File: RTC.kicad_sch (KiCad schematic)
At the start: 11 parts, among them J12 RTC Battery Port, J13 RTC Battery Conn, J7 Molex 470531000, U1 RTC PCF8563T, U10 Fan PWM Controller, Y6 ECS-.327-6

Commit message: moved some stuff around
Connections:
- net +12V_PWR renamed +24V_PWR
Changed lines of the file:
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@@
 		)
 	)
-	(hierarchical_label "+12V_PWR"
+	(hierarchical_label "+24V_PWR"
 		(shape input)
 		(at 233.68 118.11 180)

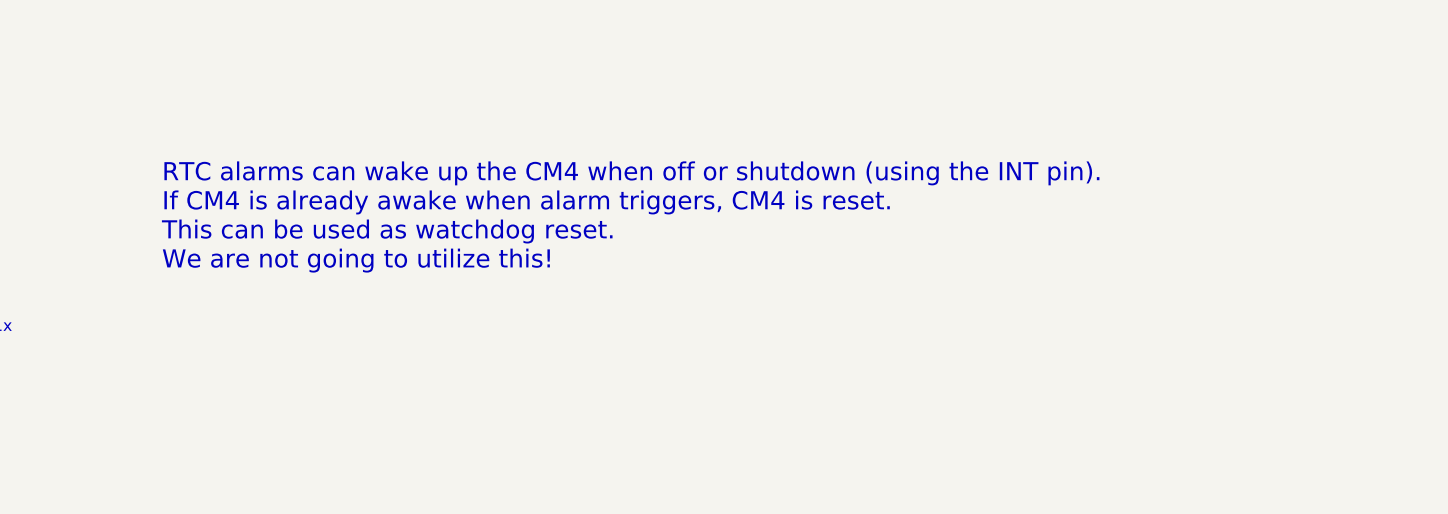
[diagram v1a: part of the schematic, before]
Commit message: Migrate to USB C and added some ESD protections on Vbus; might still have some issues
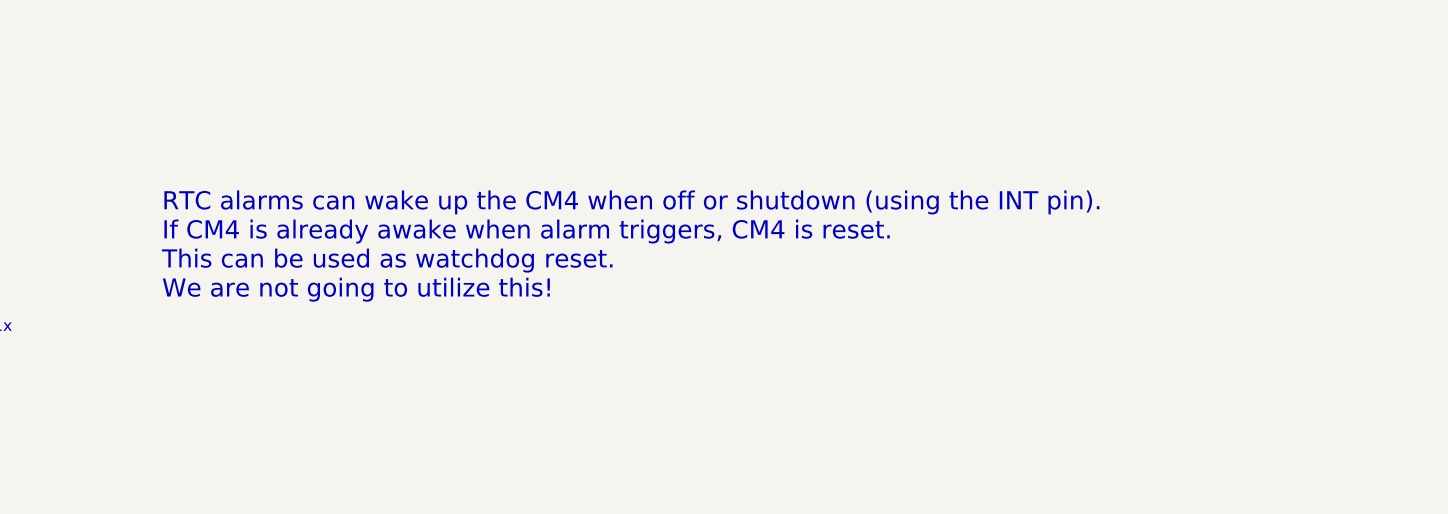
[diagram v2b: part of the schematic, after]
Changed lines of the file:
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@@
 (kicad_sch
-	(version 20231120)
+	(version 20250114)
 	(generator "eeschema")
-	(generator_version "8.0")
+	(generator_version "9.0")
 	(paper "A4")
+	(text "FAN connector\n"
+		(exclude_from_sim no)
+		(at 240.03 113.03 0)
+		(effects
+			(font
+				(size 1.27 1.27)
+			)
+			(justify left bottom)
+		)
+	)
+	(text "Also SMBUS alert IIC address : 0001_100x"
+		(exclude_from_sim no)
+		(at 184.1754 134.8994 0)
+		(effects
+			(font
+				(size 1.27 1.27)
+			)
+			(justify left bottom)
+		)
+	)
+	(text "IIC address : 1010_001x"
+		(exclude_from_sim no)
+		(at 91.3638 65.9638 0)
+		(effects
+			(font
+				(size 1.27 1.27)
+			)
+			(justify left bottom)
+		)
+	)
+	(text "Battery is enclosed in a non-SMD holder to mitigate vibration concerns. This is \ntechnically an off-board section that has the 2032 coin cell, the battery holder, \nand the molex connector (male)."
+		(exclude_from_sim no)
+		(at 39.37 120.65 0)
+		(effects
+			(font
+				(size 1.27 1.27)
+			)
+			(justify left)
+		)
+	)
+	(text "FAN controller"
+		(exclude_from_sim no)
+		(at 165.1 93.98 0)
+		(effects
+			(font
+				(size 2.0066 2.0066)
+			)
+			(justify left bottom)
+		)
+	)
+	(text "RTC alarms can wake up the CM4 when off or shutdown (using the INT pin).\nIf CM4 is already awake when alarm triggers, CM4 is reset.\nThis can be used as watchdog reset.\nWe are not going to utilize this!"
+		(exclude_from_sim no)
+		(at 129.032 62.23 0)
+		(effects
+			(font
+				(size 2.0066 2.0066)
+			)
+			(justify left bottom)
+		)
+	)
+	(text "RTC and RTC wakeup"
+		(exclude_from_sim no)
+		(at 58.928 34.29 0)
+		(effects
+			(font
+				(size 2.0066 2.0066)
+			)
+			(justify left bottom)
+		)
+	)
+	(text "IIC address : 0101_111x"
+		(exclude_from_sim no)
+		(at 184.15 130.81 0)
+		(effects
+			(font
+				(size 1.27 1.27)
+			)
+			(justify left bottom)
+		)
+	)
 	(junction
 		(at 207.01 120.65)
@@
 		)
 	)
-	(text "FAN connector\n"
-		(exclude_from_sim no)
-		(at 240.03 113.03 0)
-		(effects
-			(font
-				(size 1.27 1.27)
-			)
-			(justify left bottom)
-		)
-	)
-	(text "Also SMBUS alert IIC address : 0001_100x"
-		(exclude_from_sim no)
-		(at 184.1754 134.8994 0)
-		(effects
-			(font
-				(size 1.27 1.27)
-			)
-			(justify left bottom)
-		)
-	)
-	(text "IIC address : 1010_001x"
-		(exclude_from_sim no)
-		(at 91.3638 65.9638 0)
-		(effects
-			(font
-				(size 1.27 1.27)
-			)
-			(justify left bottom)
-		)
-	)
-	(text "Battery is enclosed in a non-SMD holder to mitigate vibration concerns. This is \ntechnically an off-board section that has the 2032 coin cell, the battery holder, \nand the molex connector (male)."
-		(exclude_from_sim no)
-		(at 39.37 120.65 0)
-		(effects
-			(font
-				(size 1.27 1.27)
-			)
-			(justify left)
-		)
-	)
-	(text "FAN controller"
-		(exclude_from_sim no)
-		(at 165.1 93.98 0)
-		(effects
-			(font
-				(size 2.0066 2.0066)
-			)
-			(justify left bottom)
-		)
-	)
-	(text "RTC alarms can wake up the CM4 when off or shutdown (using the INT pin).\nIf CM4 is already awake when alarm triggers, CM4 is reset.\nThis can be used as watchdog reset.\nWe are not going to utilize this!\n\n"
-		(exclude_from_sim no)
-		(at 129.032 62.23 0)
-		(effects
-			(font
-				(size 2.0066 2.0066)
-			)
-			(justify left bottom)
-		)
-	)
-	(text "RTC and RTC wakeup"
-		(exclude_from_sim no)
-		(at 58.928 34.29 0)
-		(effects
-			(font
-				(size 2.0066 2.0066)
-			)
-			(justify left bottom)
-		)
-	)
-	(text "IIC address : 0101_111x"
-		(exclude_from_sim no)
-		(at 184.15 130.81 0)
-		(effects
-			(font
-				(size 1.27 1.27)
-			)
-			(justify left bottom)
-		)
-	)
 	(label "RED"
 		(at 39.37 66.04 0)
-		(fields_autoplaced yes)
 		(effects
 			(font
@@
 	(label "BLK"
 		(at 72.39 114.3 90)
-		(fields_autoplaced yes)
 		(effects
 			(font
@@
 	(label "BLK"
 		(at 39.37 68.58 0)
-		(fields_autoplaced yes)
 		(effects
 			(font
@@
 	(label "RED"
 		(at 72.39 96.52 270)
-		(fields_autoplaced yes)
 		(effects
 			(font
@@
 		(shape input)
 		(at 173.99 115.57 180)
-		(fields_autoplaced yes)
 		(effects
 			(font
@@
 		(shape input)
 		(at 173.99 118.11 180)
-		(fields_autoplaced yes)
 		(effects
 			(font
@@
 		(shape input)
 		(at 233.68 118.11 180)
-		(fields_autoplaced yes)
 		(effects
 			(font
@@
 		(shape input)
 		(at 163.83 100.33 0)
-		(fields_autoplaced yes)
 		(effects
 			(font
@@
 		(shape input)
 		(at 101.6 50.8 0)
-		(fields_autoplaced yes)
 		(effects
 			(font
@@
 		(shape input)
 		(at 36.83 40.64 180)
-		(fields_autoplaced yes)
 		(effects
 			(font
@@
 		(shape input)
 		(at 101.6 48.26 0)
-		(fields_autoplaced yes)
-		(effects
-			(font
+		(effects
+			(font

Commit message: fixed erc and removed old schematics
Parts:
- J13: footprint (none) -> CONN02_530470210_MOL
- Y6: Arrow Part Number (none) -> ECS-.327-6-16R-TR; Arrow Price/Stock (none) -> https://www.arrow.com/en/products/ecs-.327-6-16r-tr/ecs-int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; Height (none) -> 0.5; Manufacturer_Name (none) -> ECS; Manufacturer_Part_Number (none) -> ECS-.327-6-16R-TR; Mouser Part Number (none) -> 520-ECS-.327-6-16RTR; Mouser Price/Stock (none) -> https://www.mouser.co.uk/ProductDetail/ECS/ECS-.327-6-16R-T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
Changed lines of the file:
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@@
 	)
 	(symbol
-		(lib_name "GND_1")
 		(lib_id "power:GND")
 		(at 39.37 72.39 0)
@@
 			)
 		)
-		(property "Footprint" ""
+		(property "Footprint" "CONN02_530470210_MOL"
 			(at 77.47 104.14 0)
 			(effects
@@
 			)
 		)
-		(property "Datasheet" "https://www.molex.com/en-us/products/part-detail-pdf/510210200?display=pdf"
+		(property "Datasheet" "https://tools.molex.com/pdm_docs/ps/PS-51021-009.pdf"
 			(at 77.47 104.14 0)
 			(effects
@@
 			)
 		)
+		(property "Height" "0.5"
+			(at -332.69 57.15 0)
+			(effects
+				(font
+					(size 1.27 1.27)
+				)
+				(justify left top)
+				(hide yes)
+			)
+		)
+		(property "Manufacturer_Name" "ECS"
+			(at -432.69 57.15 0)
+			(effects
+				(font
+					(size 1.27 1.27)
+				)
+				(justify left top)
+				(hide yes)
+			)
+		)
+		(property "Manufacturer_Part_Number" "ECS-.327-6-16R-TR"
+			(at -532.69 57.15 0)
+			(effects
+				(font
+					(size 1.27 1.27)
+				)
+				(justify left top)
+				(hide yes)
+			)
+		)
+		(property "Mouser Part Number" "520-ECS-.327-6-16RTR"
+			(at -632.69 57.15 0)
+			(effects
+				(font
+					(size 1.27 1.27)
+				)
+				(justify left top)
+				(hide yes)
+			)
+		)
+		(property "Mouser Price/Stock" "https://www.mouser.co.uk/ProductDetail/ECS/ECS-.327-6-16R-TR?qs=hWgE7mdIu5R4lQOKQkWLTw%3D%3D"
+			(at -732.69 57.15 0)
+			(effects
+				(font
+					(size 1.27 1.27)
+				)
+				(justify left top)
+				(hide yes)
+			)
+		)
+		(property "Arrow Part Number" "ECS-.327-6-16R-TR"
+			(at -832.69 57.15 0)
+			(effects
+				(font
+					(size 1.27 1.27)
+				)
+				(justify left top)
+				(hide yes)
+			)
+		)
+		(property "Arrow Price/Stock" "https://www.arrow.com/en/products/ecs-.327-6-16r-tr/ecs-international?region=nac"
+			(at -932.69 57.15 0)
+			(effects
+				(font
+					(size 1.27 1.27)
+				)
+				(justify left top)
+				(hide yes)
+			)
+		)
 		(pin "2"
 		)
@@
 	)
 	(symbol
-		(lib_name "GND_4")
 		(lib_id "power:GND")
 		(at 82.55 66.04 0)
@@
 	)
 	(symbol
-		(lib_name "GND_1")
 		(lib_id "power:GND")
 		(at 54.61 54.61 0)
@@
 	)
 	(symbol
-		(lib_name "GND_4")
 		(lib_id "power:GND")
 		(at 240.03 132.08 0)
@@
 			)
 		)
-		(property "Datasheet" "https://www.mouser.com/datasheet/2/215/1086-1901326.pdf"
+		(property "Datasheet" "https://www.keyelco.com/product-pdf.cfm?p=14638"
 			(at 72.39 105.156 90)
 			(effects
@@
 			)
 		)
-		(property "Description" "Single-cell battery holder"
+		(property "Description" "Single-cell battery Holder 20mm 6\" leads"
 			(at 72.39 106.68 0)
 			(effects
@@
 	)
 	(symbol
-		(lib_name "PCF8563T_1")
 		(lib_id "Timer_RTC:PCF8563T")
 		(at 82.55 53.34 0)
@@
 	)
 	(symbol
-		(lib_name "GND_3")
 		(lib_id "power:GND")
 		(at 168.91 132.08 0)
@@
 			)
 		)
-		(property "Datasheet" "https://www.mouser.com/datasheet/2/447/KEM_C1002_X7R_SMD-3316098.pdf"
+		(property "Datasheet" "~"
 			(at 54.61 48.26 0)
 			(effects
@@
 			)
 		)
-		(property "Description" "Capacitor 0.1u 20%"
+		(property "Description" "Unpolarized capacitor"
 			(at 54.61 48.26 0)
 			(effects
@@
 	)
 	(symbol
-		(lib_name "530470210_1")
 		(lib_id "530470210:530470210")
 		(at 46.99 66.04 0)
@@
 			)
 		)
-		(property "Datasheet" "530470210"
+		(property "Datasheet" "https://www.molex.com/content/dam/molex/molex-dot-com/products/automated/en-us/salesdrawingpdf/530/53047/530470210_sd.pdf?inline"
 			(at 46.99 66.04 0)
 			(effects
@@
 	)
 	(symbol
-		(lib_name "GND_4")
 		(lib_id "power:GND")
 		(at 179.07 132.08 0)
@@
 			)
 		)
-		(property "Datasheet" "https://www.mouser.com/datasheet/2/447/PYu_AC_51_RoHS_L_11-3418659.pdf"
+		(property "Datasheet" "~"
 			(at 207.01 115.57 0)
 			(effects
@@
 			)
 		)
-		(property "Description" "Resistor 36K M1005 1% 125mW"
+		(property "Description" "Resistor"
 			(at 207.01 115.57 0)
 			(effects
@@
 			)
 		)
-		(property "Datasheet" "https://www.mouser.com/datasheet/2/447/KEM_C1002_X7R_SMD-3316098.pdf"
+		(property "Datasheet" "~"
 			(at 168.91 127 0)
 			(effects
@@
 			)
 		)
-		(property "Description" "Capacitor 0.1u 20%"
+		(property "Description" "Unpolarized capacitor"
 			(at 168.91 127 0)
 			(effects
@@
 			)
 		)
-		(property "Datasheet" "https://www.molex.com/en-us/products/part-detail/470531000?display=pdf"
+		(property "Datasheet" "~"
 			(at 246.38 118.11 0)
 			(effects
@@
 			)
 		)
-		(property "Description" "Connector Header Through Hole 4 position 0.100\" (2.54mm)"
+		(property "Description" "Generic connector, single row, 01x04, script generated (kicad-library-utils/schlib/autogen/connector/)"
 			(at 246.38 118.11 0)
 			(effects

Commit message: changed usb to be simpler (no inbuilt hub)
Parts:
- J12, J13: footprint CONN02_530470210_MOL -> Controls_Pi:CONN02_530470210_MOL
- Y6: Arrow Part Number ECS-.327-6-16R-TR -> (none); Arrow Price/Stock https://www.arrow.com/en/products/ecs-.327-6-16r-tr/ecs-int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 -> (none); Height 0.5 -> (none); Manufacturer_Name ECS -> (none); Manufacturer_Part_Number ECS-.327-6-16R-TR -> (none); Mouser Part Number 520-ECS-.327-6-16RTR -> (none); Mouser Price/Stock https://www.mouser.co.uk/ProductDetail/ECS/ECS-.327-6-16R-T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 -> (none)
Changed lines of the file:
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@@
 			)
 		)
-		(property "Footprint" "CONN02_530470210_MOL"
+		(property "Footprint" "Controls_Pi:CONN02_530470210_MOL"
 			(at 77.47 104.14 0)
 			(effects
@@
 		(property "P/N" "ECS-.327-6-16R-TR"
 			(at -532.69 57.15 0)
-			(effects
-				(font
-					(size 1.27 1.27)
-				)
-				(justify left top)
-				(hide yes)
-			)
-		)
-		(property "Height" "0.5"
-			(at -332.69 57.15 0)
-			(effects
-				(font
-					(size 1.27 1.27)
-				)
-				(justify left top)
-				(hide yes)
-			)
-		)
-		(property "Manufacturer_Name" "ECS"
-			(at -432.69 57.15 0)
-			(effects
-				(font
-					(size 1.27 1.27)
-				)
-				(justify left top)
-				(hide yes)
-			)
-		)
-		(property "Manufacturer_Part_Number" "ECS-.327-6-16R-TR"
-			(at -532.69 57.15 0)
-			(effects
-				(font
-					(size 1.27 1.27)
-				)
-				(justify left top)
-				(hide yes)
-			)
-		)
-		(property "Mouser Part Number" "520-ECS-.327-6-16RTR"
-			(at -632.69 57.15 0)
-			(effects
-				(font
-					(size 1.27 1.27)
-				)
-				(justify left top)
-				(hide yes)
-			)
-		)
-		(property "Mouser Price/Stock" "https://www.mouser.co.uk/ProductDetail/ECS/ECS-.327-6-16R-TR?qs=hWgE7mdIu5R4lQOKQkWLTw%3D%3D"
-			(at -732.69 57.15 0)
-			(effects
-				(font
-					(size 1.27 1.27)
-				)
-				(justify left top)
-				(hide yes)
-			)
-		)
-		(property "Arrow Part Number" "ECS-.327-6-16R-TR"
-			(at -832.69 57.15 0)
-			(effects
-				(font
-					(size 1.27 1.27)
-				)
-				(justify left top)
-				(hide yes)
-			)
-		)
-		(property "Arrow Price/Stock" "https://www.arrow.com/en/products/ecs-.327-6-16r-tr/ecs-international?region=nac"
-			(at -932.69 57.15 0)
 			(effects
 				(font
@@
 			)
 		)
-		(property "Footprint" "CONN02_530470210_MOL"
+		(property "Footprint" "Controls_Pi:CONN02_530470210_MOL"
 			(at 46.99 66.04 0)
 			(effects

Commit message: moved everything to front & 0603'd stuff
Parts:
- C20, C21: footprint Capacitor_SMD:C_0805_2012Metric -> Capacitor_SMD:C_0603_1608Metric
- R16: footprint Resistor_SMD:R_0805_2012Metric -> Resistor_SMD:R_0603_1608Metric
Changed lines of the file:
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@@
 			)
 		)
-		(property "Footprint" "Capacitor_SMD:C_0805_2012Metric"
+		(property "Footprint" "Capacitor_SMD:C_0603_1608Metric"
 			(at 55.5752 52.07 0)
 			(effects
@@
 			)
 		)
-		(property "Footprint" "Resistor_SMD:R_0805_2012Metric"
+		(property "Footprint" "Resistor_SMD:R_0603_1608Metric"
 			(at 205.232 115.57 90)
 			(effects
@@
 			)
 		)
-		(property "Footprint" "Capacitor_SMD:C_0805_2012Metric"
+		(property "Footprint" "Capacitor_SMD:C_0603_1608Metric"
 			(at 169.8752 130.81 0)
 			(effects

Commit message: changed a bunch of stuff, still have work
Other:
- note added: "Needs flyback diode"
- note added: "Something to do with mounting"
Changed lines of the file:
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@@
 	(generator_version "9.0")
 	(paper "A4")
+	(text "Something to do with mounting\n"
+		(exclude_from_sim no)
+		(at 228.854 97.536 0)
+		(effects
+			(font
+				(size 1.27 1.27)
+			)
+		)
+	)
+	(text "Needs flyback diode"
+		(exclude_from_sim no)
+		(at 227.584 100.584 0)
+		(effects
+			(font
+				(size 1.27 1.27)
+			)
+		)
+	)
 	(text "FAN connector\n"
 		(exclude_from_sim no)

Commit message: my life is horrible
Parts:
- removed BT1: Battery_Cell, symbol Device:Battery_Cell
- removed C20, C21: 100n, Capacitor_SMD:C_0603_1608Metric, symbol Device:C
- removed D6: BAT54C-7-F, Package_TO_SOT_SMD:SOT-23, symbol Diode:BAT54C
- removed J12: RTC Battery Port, Controls_Pi:CONN02_530470210_MOL, symbol 530470210:530470210
- removed J13: RTC Battery Conn, Controls_Pi:CONN02_530470210_MOL, symbol 530470210:530470210
- removed J7: Molex 470531000, Connector:FanPinHeader_1x04_P2.54mm_Vertical, symbol Connector_Generic:Conn_01x04
- removed R16: 36k, Resistor_SMD:R_0603_1608Metric, symbol Device:R
- removed U1: RTC PCF8563T, Package_SO:SOIC-8_3.9x4.9mm_P1.27mm, symbol Timer_RTC:PCF8563T
- removed U10: Fan PWM Controller, Package_SO:MSOP-8_3x3mm_P0.65mm, symbol CM4IO:EMC2301
- removed Y6: ECS-.327-6, Controls_Pi:ECS327616RTR, symbol ECS-.327-6-16R-TR:ECS-.327-6-16R-TR
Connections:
- no-connect marks 4 -> 0
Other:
- note removed: "Also SMBUS alert IIC address : 0001_100x"
- note removed: "Battery is enclosed in a non-SMD holder to mitigate vibration concerns. This is technically an off-board section that has the 2032 coin cell, the battery holder, and the molex connector (male)."
- note removed: "FAN connector"
- note removed: "FAN controller"
- note removed: "IIC address : 0101_111x"
- note removed: "IIC address : 1010_001x"
- note removed: "Needs flyback diode"
- note removed: "RTC alarms can wake up the CM4 when off or shutdown (using the INT pin). If CM4 is already awake when alarm triggers, CM4 is reset. This can be used as watchdog reset. We are not going to utilize this!"
- note removed: "RTC and RTC wakeup"
- note removed: "Something to do with mounting"
